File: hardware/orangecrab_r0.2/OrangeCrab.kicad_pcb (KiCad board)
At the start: 6 copper layers, 50.8 x 22.9 mm, 165 parts, among them J1 Conn_01x12_Male, J2 Conn_01x16_Male, J3 USB_B_Micro, J4 MicroSd, J5 JST, J6 JTAG, SW1 SW_Push, U1 FAN53541, U10 NCP115-2.5, U2 FAN53541, U3 ECP5U25, U4 MT41K64M16TW-107_J-TR, U5 BQ24232, U6 W25Q128JVP, U7 FAN53541, U8 TPS51206, U9 74HC4067BQ

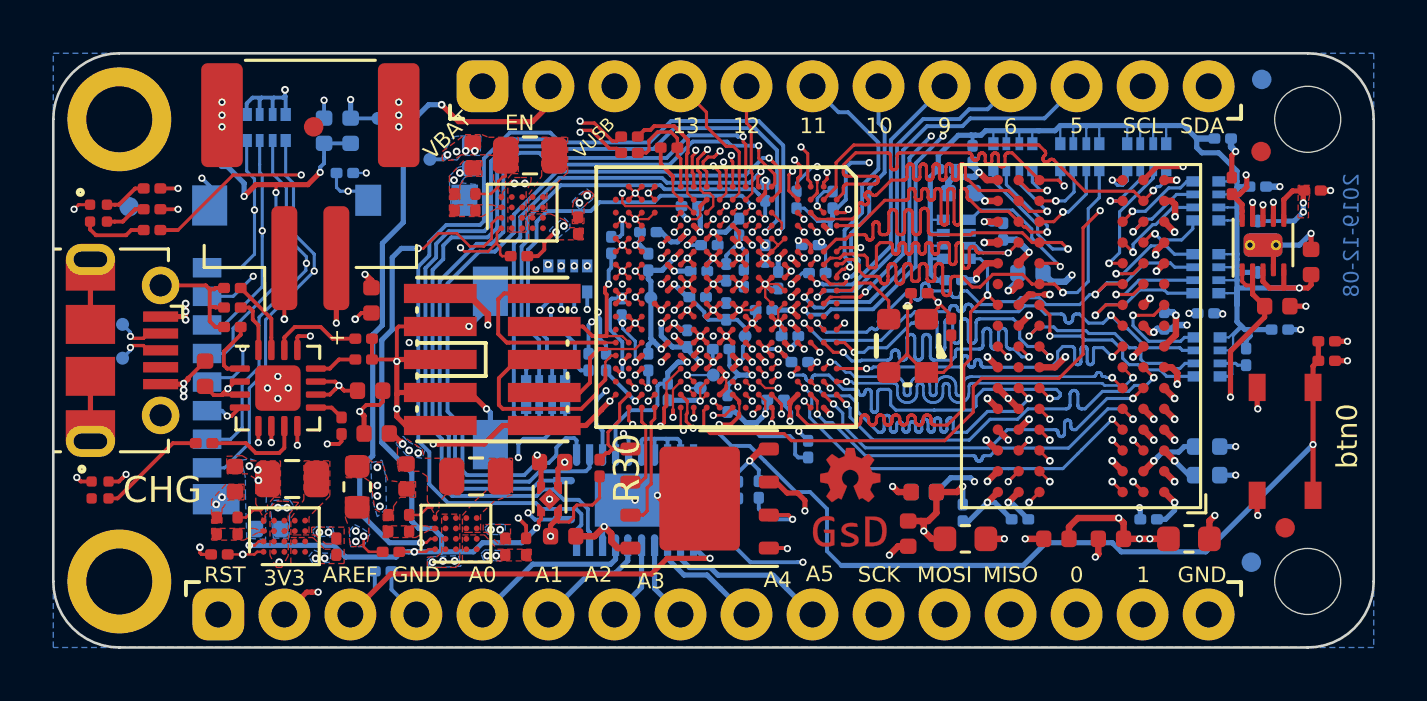
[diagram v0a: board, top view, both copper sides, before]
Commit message: hardware/orangecrab_r0.2: r0.2 Release
Prepared KiCad files for release
Create production folder
Add pdf schematic
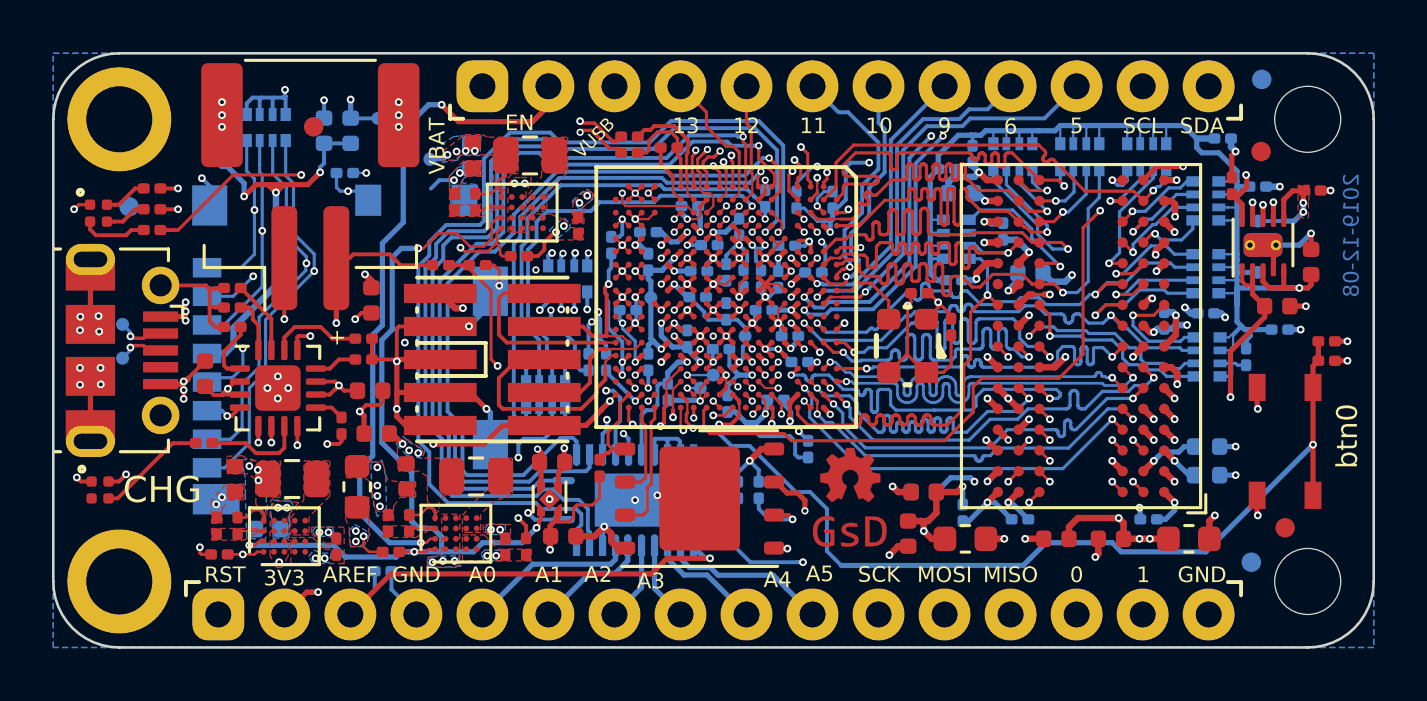
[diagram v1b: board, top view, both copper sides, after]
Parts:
- removed C73: 100nF, Capacitor_SMD:C_0201_0603Metric
- added C71: 100nF, Capacitor_SMD:C_0201_0603Metric, B.Cu at (147.2, 111.4)
- added R32: 10k, Resistor_SMD:R_0201_0603Metric, F.Cu at (149.4, 99.7)
- added R33: 10k, Resistor_SMD:R_0201_0603Metric, F.Cu at (150.8, 99.7)
- R20: value 1.5K -> 1.5k
- R22: value 4.7K -> 1.5k
- R23, R27, R30, R4: value 4.7K -> 4.7k
- R24: value 4.7K -> 3.57k
- R26, R28: value 10K -> 10k
- R31: value 1K -> 1.5k
- R7: value 1.5K -> 10k
- R8: value 1.5K -> 4.7k
- moved C62 0.98 mm to (161.7, 100.2)
- moved C68 0.90 mm to (162.7, 98.9), turned to 180 degrees
- moved C67 0.27 mm to (156.6, 101.4), turned to 0 degrees
- moved C28 0.23 mm to (161.9, 97.1)
- moved C59 0.15 mm to (163.8, 100.0)
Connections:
- U9 pad 16: P1.1V -> Net-(R32-Pad2)
- U9 pad 17: P1.35V -> P1.1V
- U9 pad 19: GND -> P1.35V
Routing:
- net Net-(R32-Pad2): track 0.00 -> 11.9 mm, vias 0 -> 2
- net /sheetIO/A1: track 20.4 -> 24.7 mm
- net GND: track 232.6 -> 236.6 mm, vias 145 -> 153
- net /sheetIO/A0: track 21.3 -> 25.3 mm
- net VBATT: track 21.9 -> 25.8 mm
- net /sheetIO/A2: track 20.7 -> 24.4 mm
- net /sheetIO/A3: track 21.7 -> 25.2 mm
- net /sheetIO/A4: track 25.2 -> 28.7 mm
- net /sheetIO/A5: track 29.7 -> 32.8 mm
- net P1.35V: track 96.3 -> 97.8 mm
- net P1.1V: track 51.4 -> 52.8 mm
- net Net-(R16-Pad1): track 0.00 -> 1.05 mm
- net Net-(R15-Pad1): track 0.00 -> 1.05 mm
- net Net-(R2-Pad1): track 0.00 -> 1.05 mm
- net Net-(C29-Pad2): track 15.1 -> 15.9 mm

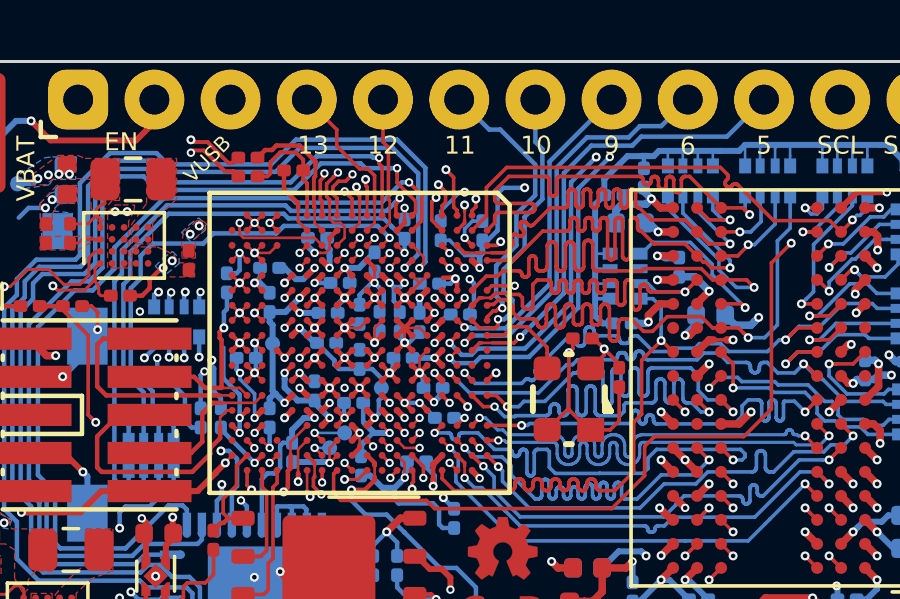
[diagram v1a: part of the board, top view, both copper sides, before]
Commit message: hardware/orangecrab-r0.2: Updated production files - Fixed fab attribute of some parts so they appear in positon file. - Regenerated outputs
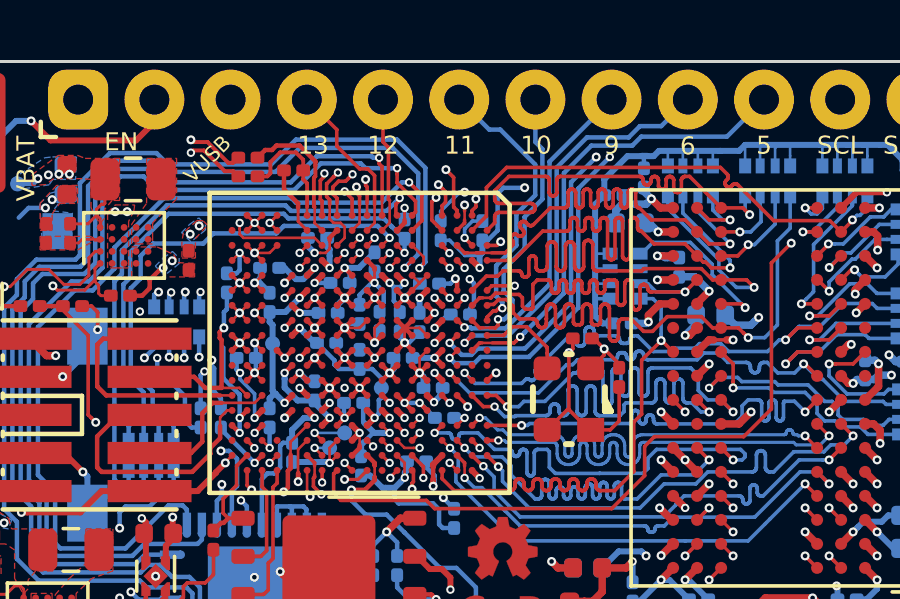
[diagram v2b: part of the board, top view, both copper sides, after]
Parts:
- OSC1: value TYETBCSANF-32.000000 -> KC2520B48.0000C10E00
- U3: value ECP5U25 -> LFE5U-25F-8MG285C
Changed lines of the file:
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@@
   )
   (setup
-    (last_trace_width 0.15)
+    (last_trace_width 0.2)
     (user_trace_width 0.089)
     (user_trace_width 0.1)
@@
       (drillshape 0)
       (scaleselection 1)
-      (outputdirectory "output/gerber/"))
+      (outputdirectory "output/"))
   )
   (net 0 "")
@@
   (module gkl_conn:molex_microsd_1040310811 (layer B.Cu)
     (at 140.427 102.875 90)
+    (attr smd)
     (fp_text reference J4 (at -0.1 14.2 -90) (layer B.SilkS) hide
       (effects (font (size 1 1) (thickness 0.15)) (justify mirror))
@@
   (module bosonFrameGrabber:csBGA_132 (layer F.Cu)
     (at 160.4 100.900001 270)
+    (attr smd)
     (fp_text reference U3 (at 0 -13.3 270) (layer F.SilkS) hide
       (effects (font (size 0 0) (thickness 0.15)))
     )
-    (fp_text value ECP5U25 (at 0 -14.3 270) (layer F.Fab) hide
+    (fp_text value LFE5U-25F-8MG285C (at 0 -14.3 270) (layer F.Fab) hide
       (effects (font (size 0 0) (thickness 0.15)))
     )
@@
   (module gkl_conn:FTSH-105-XX-X-DV (layer F.Cu)
     (at 151.4 103.300001 90)
+    (attr smd)
     (fp_text reference J6 (at 0 4.5 90) (layer F.Fab) hide
       (effects (font (size 1 1) (thickness 0.15)))
@@
   (module gkl_logos:oshw_small (layer F.Cu)
     (at 165.177 107.775)
+    (attr virtual)
     (fp_text reference G*** (at 0 0) (layer F.SilkS) hide
       (effects (font (size 0.127 0.127) (thickness 0.000001)))
@@
   (module gkl_led:0404LED_RGB (layer F.Cu)
     (at 136.25 97.67 270)
+    (attr smd)
     (fp_text reference D1 (at 0.1 -1.3 90) (layer F.SilkS) hide
       (effects (font (size 1 1) (thickness 0.15)))
@@
   (module gkl_led:0404LED_RGB (layer F.Cu)
     (at 136.31 108.32 270)
+    (attr smd)
     (fp_text reference D2 (at 0.1 -1.3 90) (layer F.SilkS) hide
       (effects (font (size 1 1) (thickness 0.15)))
@@
   (module gkl_time:Oscilator_2.5x2.0 (layer F.Cu)
     (at 167.377 102.775 90)
+    (attr smd)
     (fp_text reference OSC1 (at 0.7 -2.1 90) (layer F.SilkS) hide
       (effects (font (size 1 1) (thickness 0.15)))
     )
-    (fp_text value TYETBCSANF-32.000000 (at 0 -0.1 90) (layer F.Fab) hide
+    (fp_text value KC2520B48.0000C10E00 (at 0 -0.1 90) (layer F.Fab) hide
       (effects (font (size 1 1) (thickness 0.15)))
     )
@@
   (module LOGO (layer F.Cu)
     (at 165.152 110)
+    (attr virtual)
     (fp_text reference G*** (at 0 0) (layer F.SilkS) hide
       (effects (font (size 0 0) (thickness 0.15)))
@@
   (via (at 162.852 105.675) (size 0.3) (drill 0.15) (layers F.Cu B.Cu) (net 143))
   (segment (start 164.599999 97.6) (end 164.471096 97.728903) (width 0.2) (layer In3.Cu) (net 143))
-  (segment (start 163.037001 98.864999) (end 163.177 98.725) (width 0.2) (layer In2.Cu) (net 143))
-  (segment (start 163.001999 98.900001) (end 163.037001 98.864999) (width 0.2) (layer In2.Cu) (net 143))
   (segment (start 163.557411 97.557875) (end 163.241664 97.557875) (width 0.2) (layer In3.Cu) (net 143))
   (segment (start 163.05 97.749539) (end 163.05 98.598) (width 0.2) (layer In3.Cu) (net 143))
@@
   (segment (start 163.05 98.598) (end 163.177 98.725) (width 0.2) (layer In3.Cu) (net 143))
   (segment (start 163.241664 97.557875) (end 163.05 97.749539) (width 0.2) (layer In3.Cu) (net 143))
-  (segment (start 161.9 98.900001) (end 163.001999 98.900001) (width 0.2) (layer In2.Cu) (net 143))
   (segment (start 164.8 94.400001) (end 165.127 94.727001) (width 0.2) (layer In3.Cu) (net 143))
   (segment (start 164.599999 97.150002) (end 164.599999 97.6) (width 0.2) (layer In3.Cu) (net 143))
@@
   (segment (start 158.229999 94.400001) (end 164.8 94.400001) (width 0.2) (layer In3.Cu) (net 143))
   (segment (start 165.127 94.727001) (end 165.127 96.623001) (width 0.2) (layer In3.Cu) (net 143))
-  (segment (start 163.65 99.150001) (end 163.65 98.898) (width 0.15) (layer F.Cu) (net 143))
-  (segment (start 163.477 98.725) (end 163.177 98.725) (width 0.15) (layer F.Cu) (net 143))
-  (segment (start 163.65 98.898) (end 163.477 98.725) (width 0.15) (layer F.Cu) (net 143))
   (segment (start 161.15 98.650001) (end 161.4 98.900001) (width 0.2) (layer F.Cu) (net 143))
   (segment (start 161.65 98.650001) (end 161.9 98.900001) (width 0.2) (layer F.Cu) (net 143))
@@
   (segment (start 163.4279 98.9241) (end 163.593 98.759) (width 0.15) (layer B.Cu) (net 143))
   (segment (start 163.0494 98.9241) (end 163.4279 98.9241) (width 0.15) (layer B.Cu) (net 143))
+  (segment (start 163.65 98.816) (end 163.593 98.759) (width 0.15) (layer F.Cu) (net 143))
+  (segment (start 163.65 99.150001) (end 163.65 98.816) (width 0.15) (layer F.Cu) (net 143))
+  (segment (start 161.9 98.900001) (end 163.001999 98.900001) (width 0.2) (layer In2.Cu) (net 143))
+  (segment (start 163.1612 98.759) (end 163.1104 98.8098) (width 0.2) (layer In2.Cu) (net 143))
+  (segment (start 163.593 98.759) (end 163.1612 98.759) (width 0.2) (layer In2.Cu) (net 143))
+  (segment (start 163.001999 98.900001) (end 163.1104 98.8098) (width 0.2) (layer In2.Cu) (net 143))
   (via (at 150.177 99) (size 0.3) (drill 0.15) (layers F.Cu B.Cu) (net 144))
   (via (at 180.650007 97.255469) (size 0.3) (drill 0.15) (layers F.Cu B.Cu) (net 144))

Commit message: hw.r0_2: DFM changes to stencil layer
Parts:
- C1, C10, C14, C19, C2, C20, C25, C26, C27, C28, C30, C31, C32, C33, C38, C39, C4, C40, C41, C42, C43, C44, C45, C48, C49, C5, C50, C51, C52, C53, C54, C55, C56, C57, C58, C59, C60, C61, C62, C63, C64, C65, C66, C67, C68, C69, C70, C71, C74, C75, C76, C9: footprint Capacitor_SMD:C_0201_0603Metric -> gkl_misc:C_0201_0603Metric
- R1, R10, R11, R12, R13, R14, R15, R16, R17, R18, R2, R20, R21, R22, R23, R24, R25, R26, R27, R28, R29, R3, R30, R31, R32, R33, R4, R5, R6, R7, R8, R9: footprint Resistor_SMD:R_0201_0603Metric -> gkl_misc:R_0201_0603Metric
